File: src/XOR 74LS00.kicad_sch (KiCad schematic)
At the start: 5 parts

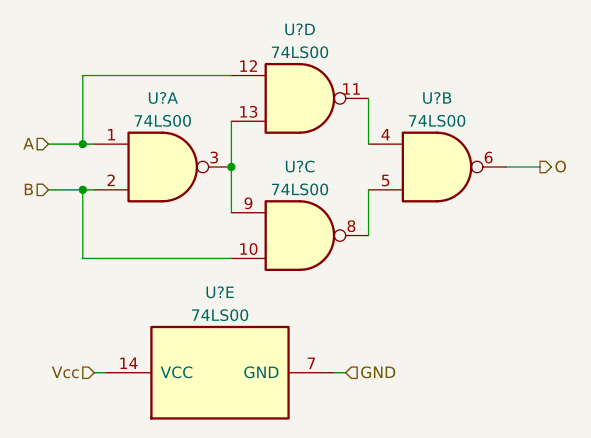
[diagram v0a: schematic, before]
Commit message: simplify circuit diagram. Remove unecessary features; Split board into two components|
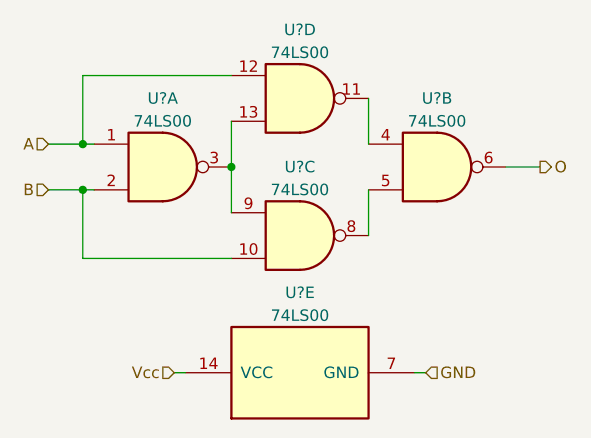
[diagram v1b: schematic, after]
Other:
- moved on the sheet: U?E
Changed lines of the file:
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@@
 (kicad_sch (version 20230121) (generator eeschema)
   (paper "A4")
+  (title_block
+    (comment 4 "Wire gauge: 1mm² / 18AWG")
+  )
   (junction (at 123.19 93.98) (diameter 0) (color 0 0 0 0)
   )
@@
     (stroke (width 0) (type default))
   )
-  (wire (pts (xy 152.4 114.3) (xy 151.13 114.3))
+  (wire (pts (xy 161.29 114.3) (xy 160.02 114.3))
     (stroke (width 0) (type default))
   )
@@
     (stroke (width 0) (type default))
   )
-  (wire (pts (xy 124.46 114.3) (xy 125.73 114.3))
+  (wire (pts (xy 133.35 114.3) (xy 134.62 114.3))
     (stroke (width 0) (type default))
   )
@@
     (stroke (width 0) (type default))
   )
-  (hierarchical_label "GND" (shape input) (at 152.4 114.3 0) (fields_autoplaced)
+  (hierarchical_label "GND" (shape input) (at 161.29 114.3 0) (fields_autoplaced)
     (effects (font (size 1.27 1.27)) (justify left))
   )
@@
     (effects (font (size 1.27 1.27)) (justify right))
   )
-  (hierarchical_label "Vcc" (shape input) (at 124.46 114.3 180) (fields_autoplaced)
+  (hierarchical_label "Vcc" (shape input) (at 133.35 114.3 180) (fields_autoplaced)
     (effects (font (size 1.27 1.27)) (justify right))
   )
@@
           (reference "U?") (unit 1)
         )
-        (path "/e63e39d7-6ac0-4ffd-8aa3-1841a4541b55/5d40715c-dfc9-4b95-9cc7-adbd4b609d9b/86972ad5-794a-4561-975c-ce46d2d4ed52"
+        (path "/e63e39d7-6ac0-4ffd-8aa3-1841a4541b55/2796a2e7-5881-4f63-b03e-84af5d47e27a/66d407c1-8bd9-4e07-b6de-9b429e179811"
           (reference "U2") (unit 1)
         )
@@
     )
   )
-  (symbol (lib_id "74xx:74LS00") (at 138.43 114.3 90) (unit 5)
-    (in_bom yes) (on_board yes) (dnp no) (fields_autoplaced)
-    (property "Reference" "U?" (at 138.43 105.41 90)
-      (effects (font (size 1.27 1.27)))
-    )
-    (property "Value" "74LS00" (at 138.43 107.95 90)
-      (effects (font (size 1.27 1.27)))
-    )
-    (property "Footprint" "Package_DIP:DIP-14_W7.62mm_Socket_LongPads" (at 138.43 114.3 0)
-      (effects (font (size 1.27 1.27)) hide)
-    )
-    (property "Datasheet" "http://www.ti.com/lit/gpn/sn74ls00" (at 138.43 114.3 0)
+  (symbol (lib_id "74xx:74LS00") (at 147.32 114.3 90) (unit 5)
+    (in_bom yes) (on_board yes) (dnp no) (fields_autoplaced)
+    (property "Reference" "U?" (at 147.32 105.41 90)
+      (effects (font (size 1.27 1.27)))
+    )
+    (property "Value" "74LS00" (at 147.32 107.95 90)
+      (effects (font (size 1.27 1.27)))
+    )
+    (property "Footprint" "Package_DIP:DIP-14_W7.62mm_Socket_LongPads" (at 147.32 114.3 0)
+      (effects (font (size 1.27 1.27)) hide)
+    )
+    (property "Datasheet" "http://www.ti.com/lit/gpn/sn74ls00" (at 147.32 114.3 0)
       (effects (font (size 1.27 1.27)) hide)
     )
@@
           (reference "U?") (unit 5)
         )
-        (path "/e63e39d7-6ac0-4ffd-8aa3-1841a4541b55/5d40715c-dfc9-4b95-9cc7-adbd4b609d9b/86972ad5-794a-4561-975c-ce46d2d4ed52"
+        (path "/e63e39d7-6ac0-4ffd-8aa3-1841a4541b55/2796a2e7-5881-4f63-b03e-84af5d47e27a/66d407c1-8bd9-4e07-b6de-9b429e179811"
           (reference "U2") (unit 5)
         )
@@
           (reference "U?") (unit 4)
         )
-        (path "/e63e39d7-6ac0-4ffd-8aa3-1841a4541b55/5d40715c-dfc9-4b95-9cc7-adbd4b609d9b/86972ad5-794a-4561-975c-ce46d2d4ed52"
+        (path "/e63e39d7-6ac0-4ffd-8aa3-1841a4541b55/2796a2e7-5881-4f63-b03e-84af5d47e27a/66d407c1-8bd9-4e07-b6de-9b429e179811"
           (reference "U2") (unit 4)
         )
@@
           (reference "U?") (unit 2)
         )
-        (path "/e63e39d7-6ac0-4ffd-8aa3-1841a4541b55/5d40715c-dfc9-4b95-9cc7-adbd4b609d9b/86972ad5-794a-4561-975c-ce46d2d4ed52"
+        (path "/e63e39d7-6ac0-4ffd-8aa3-1841a4541b55/2796a2e7-5881-4f63-b03e-84af5d47e27a/66d407c1-8bd9-4e07-b6de-9b429e179811"
           (reference "U2") (unit 2)
         )
@@
           (reference "U?") (unit 3)
         )
-        (path "/e63e39d7-6ac0-4ffd-8aa3-1841a4541b55/5d40715c-dfc9-4b95-9cc7-adbd4b609d9b/86972ad5-794a-4561-975c-ce46d2d4ed52"
+        (path "/e63e39d7-6ac0-4ffd-8aa3-1841a4541b55/2796a2e7-5881-4f63-b03e-84af5d47e27a/66d407c1-8bd9-4e07-b6de-9b429e179811"
           (reference "U2") (unit 3)
         )
